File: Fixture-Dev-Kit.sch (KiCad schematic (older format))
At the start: 0 parts

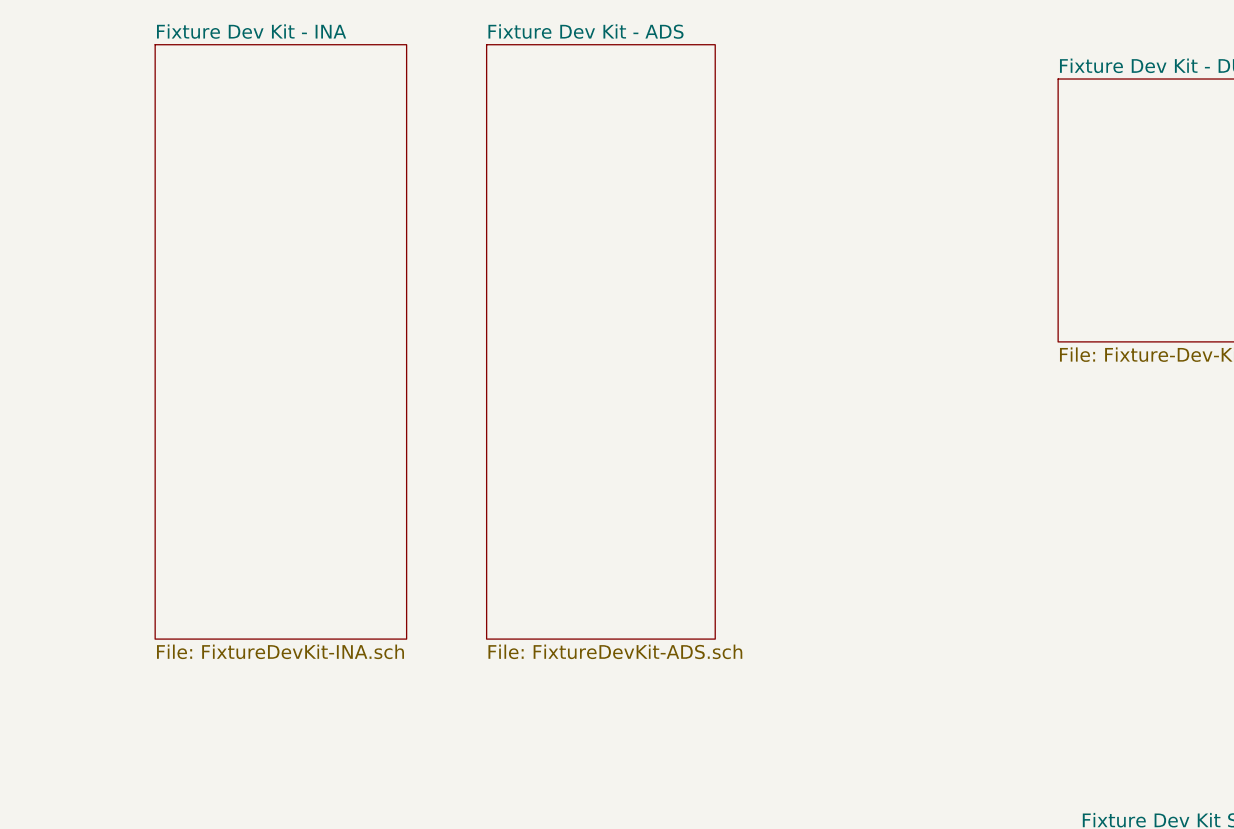
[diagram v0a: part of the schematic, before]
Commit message: adding the dummy load circuit
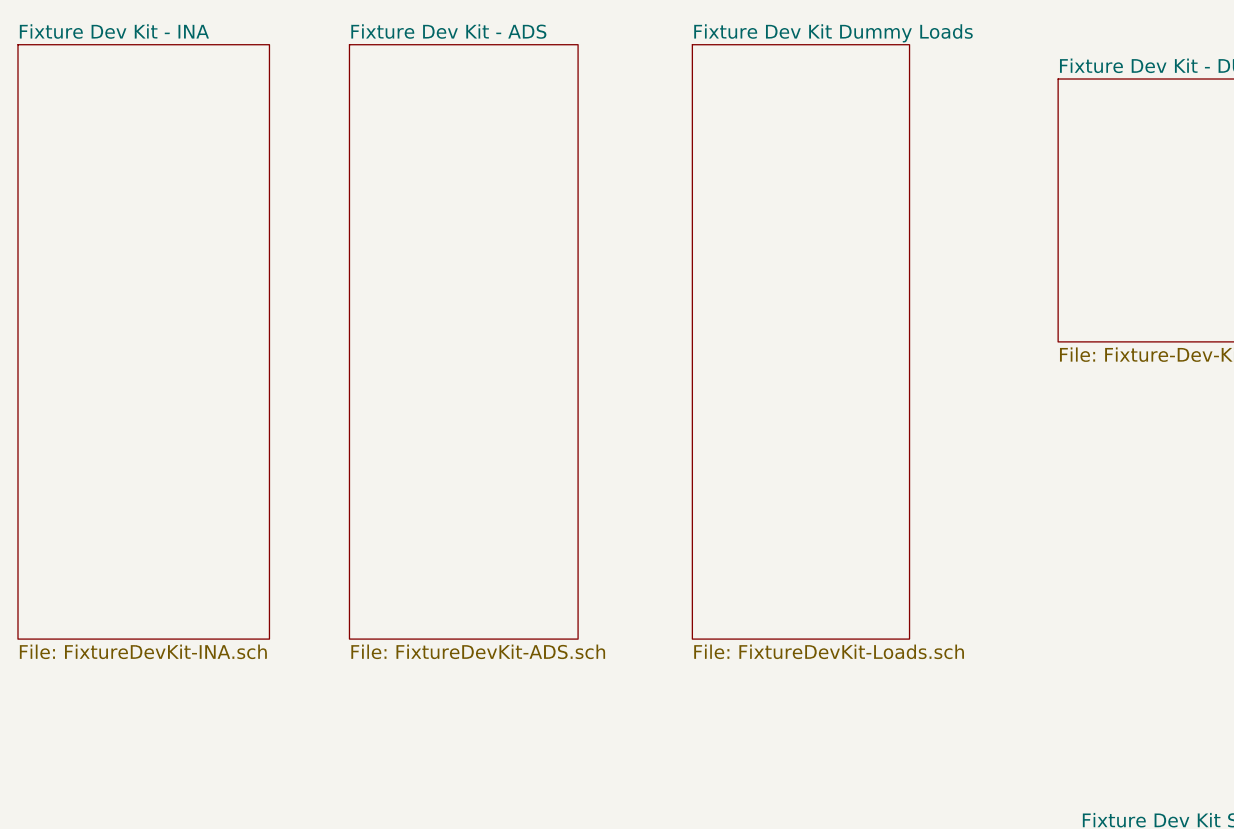
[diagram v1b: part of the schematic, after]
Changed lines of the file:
@@
 $Descr A4 11693 8268
 encoding utf-8
-Sheet 1 5
+Sheet 1 6
 Title ""
 Date ""
@@
 $EndSheet
 $Sheet
-S 4050 1100 1100 2600
+S 3450 1100 1100 2600
 U 59EE50B5
 F0 "Fixture Dev Kit - INA" 60
@@
 $EndSheet
 $Sheet
-S 5500 1100 1000 2600
+S 4900 1100 1000 2600
 U 59EEAF92
 F0 "Fixture Dev Kit - ADS" 60
 F1 "FixtureDevKit-ADS.sch" 60
 $EndSheet
+$Sheet
+S 6400 1100 950  2600
+U 59EE63FB
+F0 "Fixture Dev Kit Dummy Loads" 60
+F1 "FixtureDevKit-Loads.sch" 60
+$EndSheet
 $EndSCHEMATC

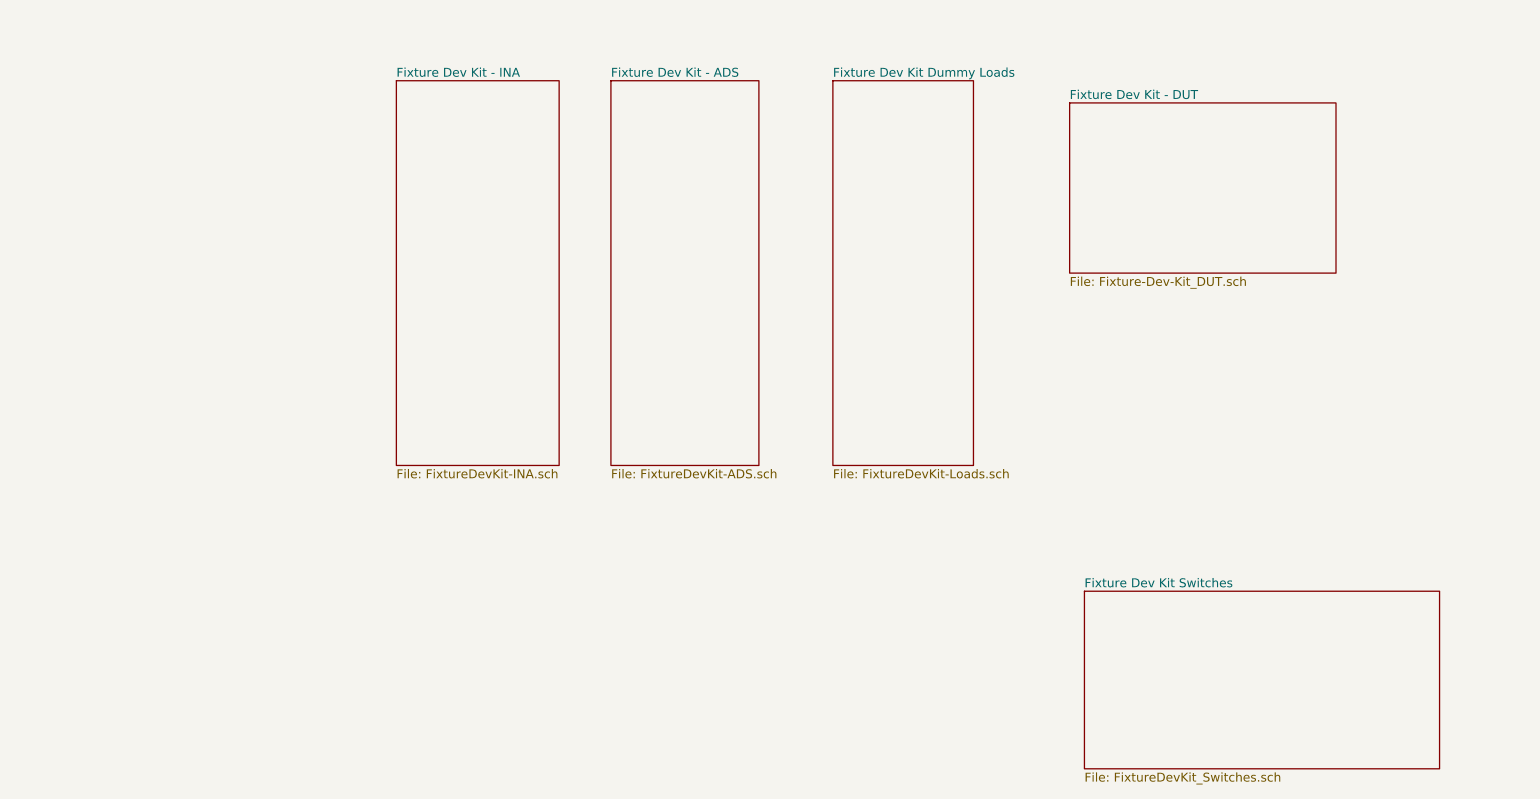
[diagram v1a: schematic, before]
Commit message: adding LED and Button circuit
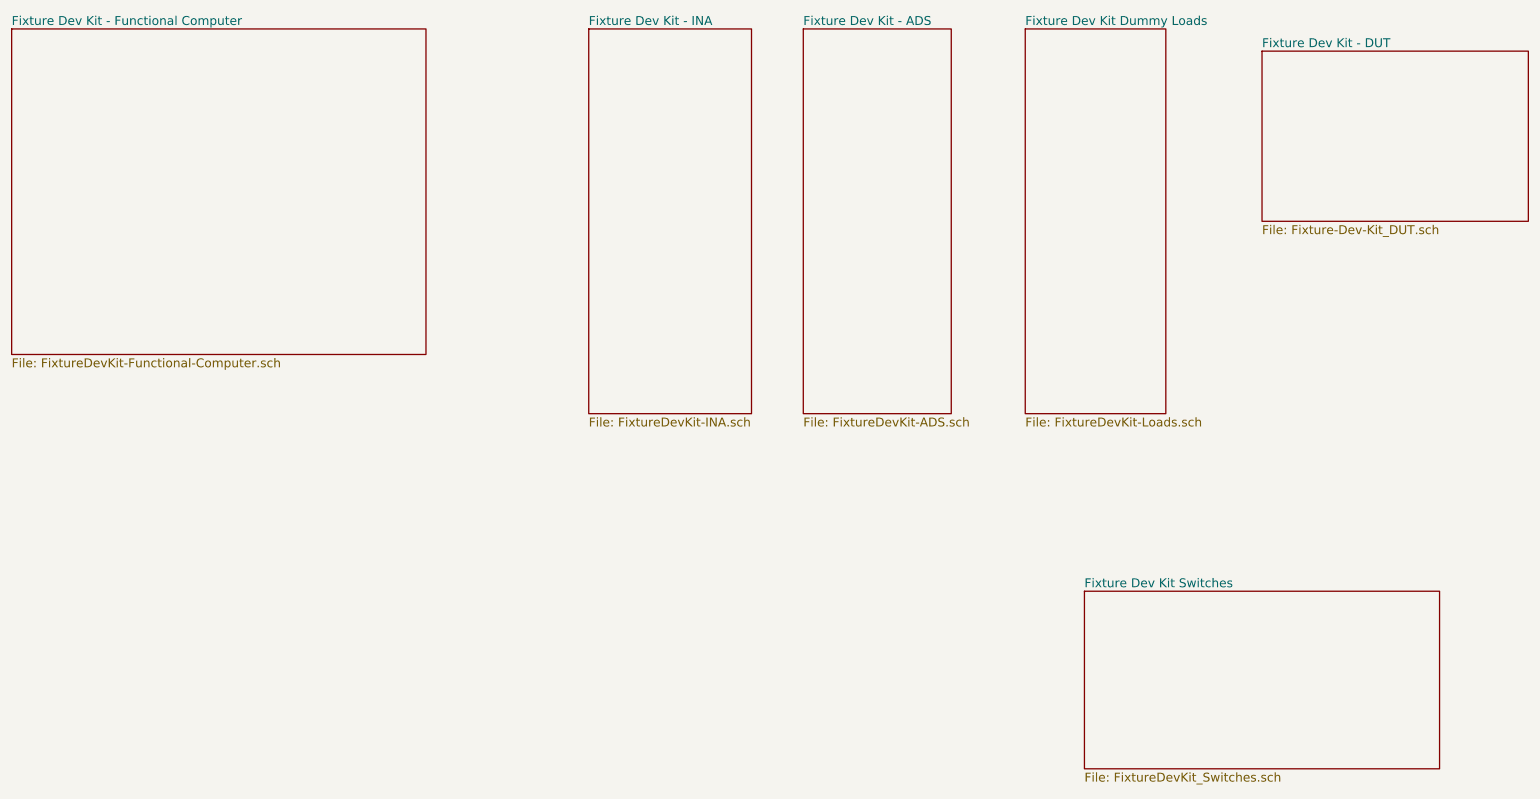
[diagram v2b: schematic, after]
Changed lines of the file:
@@
 $Descr A4 11693 8268
 encoding utf-8
-Sheet 1 6
+Sheet 1 7
 Title ""
 Date ""
@@
 $EndDescr
 $Sheet
-S 8000 1250 1800 1150
+S 9300 900  1800 1150
 U 59EE1B11
 F0 "Fixture Dev Kit - DUT" 60
@@
 $EndSheet
 $Sheet
-S 3450 1100 1100 2600
+S 4750 750  1100 2600
 U 59EE50B5
 F0 "Fixture Dev Kit - INA" 60
@@
 $EndSheet
 $Sheet
-S 4900 1100 1000 2600
+S 6200 750  1000 2600
 U 59EEAF92
 F0 "Fixture Dev Kit - ADS" 60
@@
 $EndSheet
 $Sheet
-S 6400 1100 950  2600
+S 7700 750  950  2600
 U 59EE63FB
 F0 "Fixture Dev Kit Dummy Loads" 60
 F1 "FixtureDevKit-Loads.sch" 60
 $EndSheet
+$Sheet
+S 850  750  2800 2200
+U 59EE6806
+F0 "Fixture Dev Kit - Functional Computer" 60
+F1 "FixtureDevKit-Functional-Computer.sch" 60
+$EndSheet
 $EndSCHEMATC
